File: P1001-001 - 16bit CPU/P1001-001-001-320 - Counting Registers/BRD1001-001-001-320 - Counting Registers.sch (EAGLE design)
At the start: 16 parts, among them IC1 74HC192D, IC12 74AC245DW, IC2 74HC192D, IC27 MEGA8535-A, IC3 74HC192D, IC4 74HC192D, IC5 74ALS04D, IC7 74AC245DW, J1 22-27-2041-04

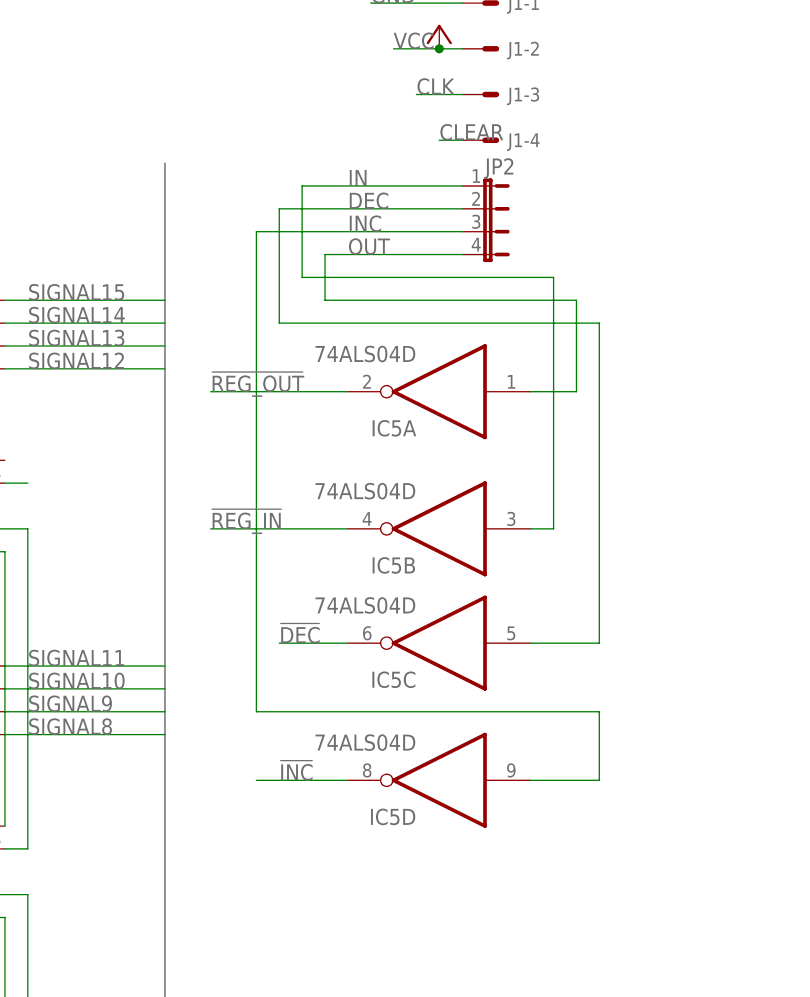
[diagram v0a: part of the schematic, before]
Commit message: Added the simple reg, cleaned things up
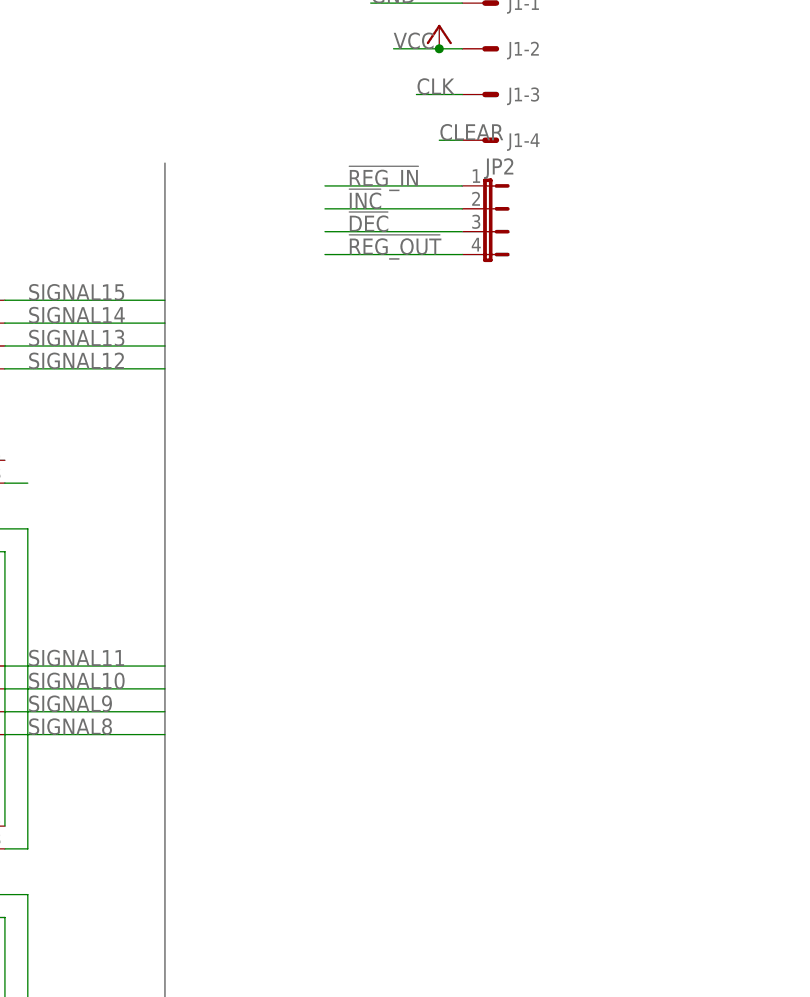
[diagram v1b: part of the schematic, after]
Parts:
- removed IC5: 74ALS04D, 74xx-us:74ALS04D
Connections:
- removed net DEC: IC5C.I, JP2.2
- removed net IN: IC5B.I, JP2.1
- removed net INC: IC5D.I, JP2.3
- removed net OUT: IC5A.I, JP2.4
- net !DEC: now also JP2.3; no longer IC5C.O
- net !INC: now also JP2.2; no longer IC5D.O
- net !REG_IN: now also JP2.1; no longer IC5B.O
- net !REG_OUT: now also JP2.4; no longer IC5A.O
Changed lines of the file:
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@@
 <class number="0" name="default" width="0" drill="0">
+</class>
+<class number="1" name="power" width="0.4572" drill="0">
 </class>
 </classes>
@@
 <part name="IC3" library="74xx-eu" library_urn="urn:adsk.eagle:library:85" deviceset="74*192" device="D" package3d_urn="urn:adsk.eagle:package:2010/1" technology="HC"/>
 <part name="IC4" library="74xx-eu" library_urn="urn:adsk.eagle:library:85" deviceset="74*192" device="D" package3d_urn="urn:adsk.eagle:package:2010/1" technology="HC"/>
-<part name="IC5" library="74xx-us" library_urn="urn:adsk.eagle:library:88" deviceset="74*04" device="D" package3d_urn="urn:adsk.eagle:package:2917/1" technology="ALS"/>
 </parts>
 <sheets>
@@
 <attribute name="VALUE" x="73.66" y="104.14" size="1.778" layer="96"/>
 </instance>
-<instance part="IC5" gate="A" x="142.24" y="119.38" smashed="yes" rot="R180">
-<attribute name="NAME" x="139.7" y="116.205" size="1.778" layer="95" rot="R180"/>
-<attribute name="VALUE" x="139.7" y="124.46" size="1.778" layer="96" rot="R180"/>
-</instance>
-<instance part="IC5" gate="B" x="142.24" y="104.14" smashed="yes" rot="R180">
-<attribute name="NAME" x="139.7" y="100.965" size="1.778" layer="95" rot="R180"/>
-<attribute name="VALUE" x="139.7" y="109.22" size="1.778" layer="96" rot="R180"/>
-</instance>
-<instance part="IC5" gate="C" x="142.24" y="91.44" smashed="yes" rot="R180">
-<attribute name="NAME" x="139.7" y="88.265" size="1.778" layer="95" rot="R180"/>
-<attribute name="VALUE" x="139.7" y="96.52" size="1.778" layer="96" rot="R180"/>
-</instance>
-<instance part="IC5" gate="D" x="142.24" y="76.2" smashed="yes" rot="R180">
-<attribute name="NAME" x="139.7" y="73.025" size="1.778" layer="95" rot="R180"/>
-<attribute name="VALUE" x="139.7" y="81.28" size="1.778" layer="96" rot="R180"/>
-</instance>
 </instances>
 <busses>
@@
 </segment>
 <segment>
-<pinref part="IC5" gate="A" pin="O"/>
-<wire x1="132.08" y1="119.38" x2="116.84" y2="119.38" width="0.1524" layer="91"/>
-<label x="116.84" y="119.38" size="1.778" layer="95"/>
+<pinref part="JP2" gate="G$1" pin="4"/>
+<wire x1="144.78" y1="134.62" x2="129.54" y2="134.62" width="0.1524" layer="91"/>
+<label x="132.08" y="134.62" size="1.778" layer="95"/>
 </segment>
 </net>
@@
 </segment>
 <segment>
-<pinref part="IC5" gate="B" pin="O"/>
-<wire x1="132.08" y1="104.14" x2="116.84" y2="104.14" width="0.1524" layer="91"/>
-<label x="116.84" y="104.14" size="1.778" layer="95"/>
-</segment>
-</net>
-<net name="GND" class="0">
+<pinref part="JP2" gate="G$1" pin="1"/>
+<wire x1="144.78" y1="142.24" x2="129.54" y2="142.24" width="0.1524" layer="91"/>
+<label x="132.08" y="142.24" size="1.778" layer="95"/>
+</segment>
+</net>
+<net name="GND" class="1">
 <segment>
 <pinref part="GND1" gate="1" pin="GND"/>
@@
 </segment>
 </net>
-<net name="VCC" class="0">
+<net name="VCC" class="1">
 <segment>
 <pinref part="J1" gate="-2" pin="S"/>
@@
 </segment>
 </net>
-<net name="DEC" class="0">
-<segment>
-<pinref part="JP2" gate="G$1" pin="2"/>
-<wire x1="144.78" y1="139.7" x2="124.46" y2="139.7" width="0.1524" layer="91"/>
-<label x="132.08" y="139.7" size="1.778" layer="95"/>
-<wire x1="124.46" y1="139.7" x2="124.46" y2="127" width="0.1524" layer="91"/>
-<wire x1="124.46" y1="127" x2="160.02" y2="127" width="0.1524" layer="91"/>
-<pinref part="IC5" gate="C" pin="I"/>
-<wire x1="160.02" y1="127" x2="160.02" y2="91.44" width="0.1524" layer="91"/>
-<wire x1="160.02" y1="91.44" x2="152.4" y2="91.44" width="0.1524" layer="91"/>
-</segment>
-</net>
-<net name="INC" class="0">
-<segment>
-<pinref part="JP2" gate="G$1" pin="3"/>
-<wire x1="144.78" y1="137.16" x2="121.92" y2="137.16" width="0.1524" layer="91"/>
-<label x="132.08" y="137.16" size="1.778" layer="95"/>
-<wire x1="121.92" y1="137.16" x2="121.92" y2="83.82" width="0.1524" layer="91"/>
-<wire x1="121.92" y1="83.82" x2="160.02" y2="83.82" width="0.1524" layer="91"/>
-<wire x1="160.02" y1="83.82" x2="160.02" y2="76.2" width="0.1524" layer="91"/>
-<pinref part="IC5" gate="D" pin="I"/>
-<wire x1="160.02" y1="76.2" x2="152.4" y2="76.2" width="0.1524" layer="91"/>
-</segment>
-</net>
 <net name="N$1" class="0">
 <segment>
 <pinref part="IC4" gate="A" pin="BO"/>
 <wire x1="96.52" y1="109.22" x2="93.98" y2="109.22" width="0.1524" layer="91"/>
-</segment>
-</net>
-<net name="IN" class="0">
-<segment>
-<pinref part="JP2" gate="G$1" pin="1"/>
-<wire x1="144.78" y1="142.24" x2="127" y2="142.24" width="0.1524" layer="91"/>
-<label x="132.08" y="142.24" size="1.778" layer="95"/>
-<wire x1="127" y1="142.24" x2="127" y2="132.08" width="0.1524" layer="91"/>
-<wire x1="127" y1="132.08" x2="154.94" y2="132.08" width="0.1524" layer="91"/>
-<wire x1="154.94" y1="132.08" x2="154.94" y2="104.14" width="0.1524" layer="91"/>
-<pinref part="IC5" gate="B" pin="I"/>
-<wire x1="154.94" y1="104.14" x2="152.4" y2="104.14" width="0.1524" layer="91"/>
-</segment>
-</net>
-<net name="OUT" class="0">
-<segment>
-<pinref part="JP2" gate="G$1" pin="4"/>
-<wire x1="144.78" y1="134.62" x2="129.54" y2="134.62" width="0.1524" layer="91"/>
-<label x="132.08" y="134.62" size="1.778" layer="95"/>
-<wire x1="129.54" y1="134.62" x2="129.54" y2="129.54" width="0.1524" layer="91"/>
-<wire x1="129.54" y1="129.54" x2="157.48" y2="129.54" width="0.1524" layer="91"/>
-<wire x1="157.48" y1="129.54" x2="157.48" y2="119.38" width="0.1524" layer="91"/>
-<pinref part="IC5" gate="A" pin="I"/>
-<wire x1="157.48" y1="119.38" x2="152.4" y2="119.38" width="0.1524" layer="91"/>
 </segment>
 </net>
@@
 </segment>
 <segment>
-<pinref part="IC5" gate="C" pin="O"/>
-<wire x1="132.08" y1="91.44" x2="124.46" y2="91.44" width="0.1524" layer="91"/>
-<label x="124.46" y="91.44" size="1.778" layer="95"/>
+<pinref part="JP2" gate="G$1" pin="3"/>
+<wire x1="144.78" y1="137.16" x2="129.54" y2="137.16" width="0.1524" layer="91"/>
+<label x="132.08" y="137.16" size="1.778" layer="95"/>
 </segment>
 </net>
@@
 </segment>
 <segment>
-<pinref part="IC5" gate="D" pin="O"/>
-<wire x1="132.08" y1="76.2" x2="121.92" y2="76.2" width="0.1524" layer="91"/>
-<label x="124.46" y="76.2" size="1.778" layer="95"/>
-</segment>
-</net>
+<pinref part="JP2" gate="G$1" pin="2"/>
+<wire x1="144.78" y1="139.7" x2="129.54" y2="139.7" width="0.1524" layer="91"/>
+<label x="132.08" y="139.7" size="1.778" layer="95"/>
+</segment>
+</net>

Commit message: Finished All Boards
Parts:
- added C1, C2, C3, C4: 1uF, rcl:C-USC1206
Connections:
- net GND: now also C1.2, C2.2, C3.2, C4.2
- net VCC: now also C1.1, C2.1, C3.1, C4.1

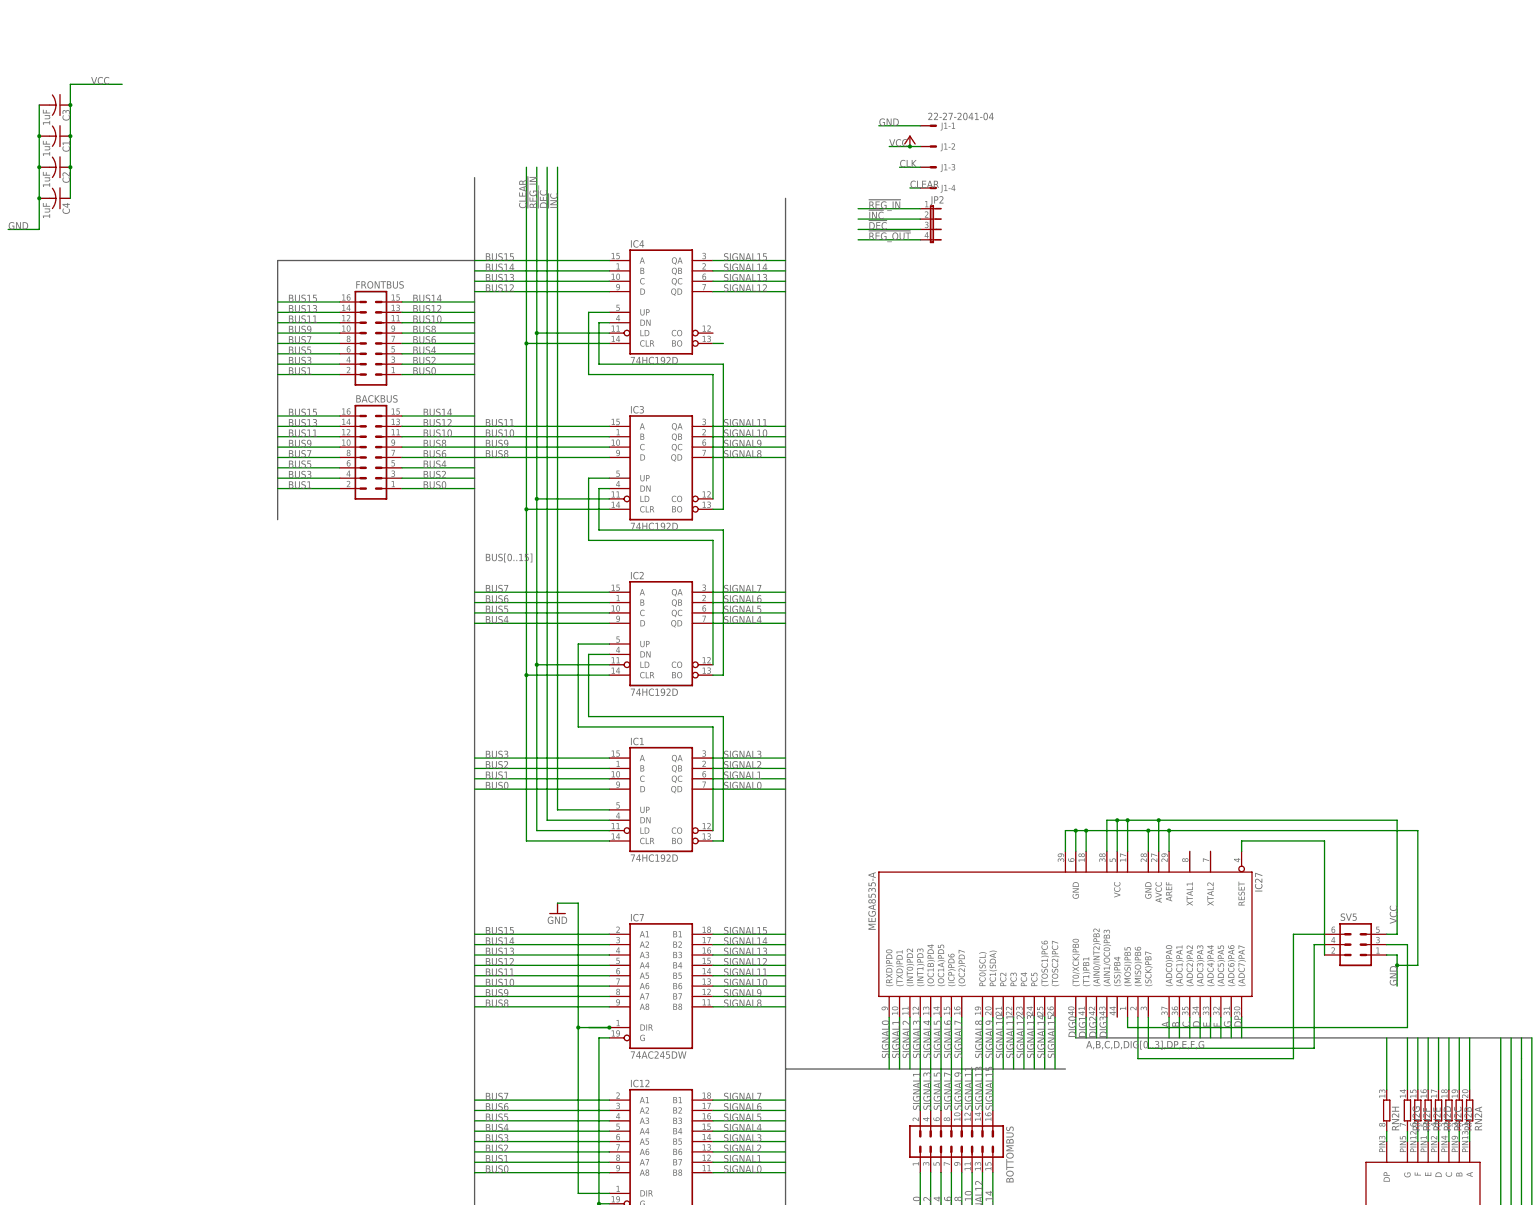
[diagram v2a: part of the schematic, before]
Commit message: fix the 16 register problem
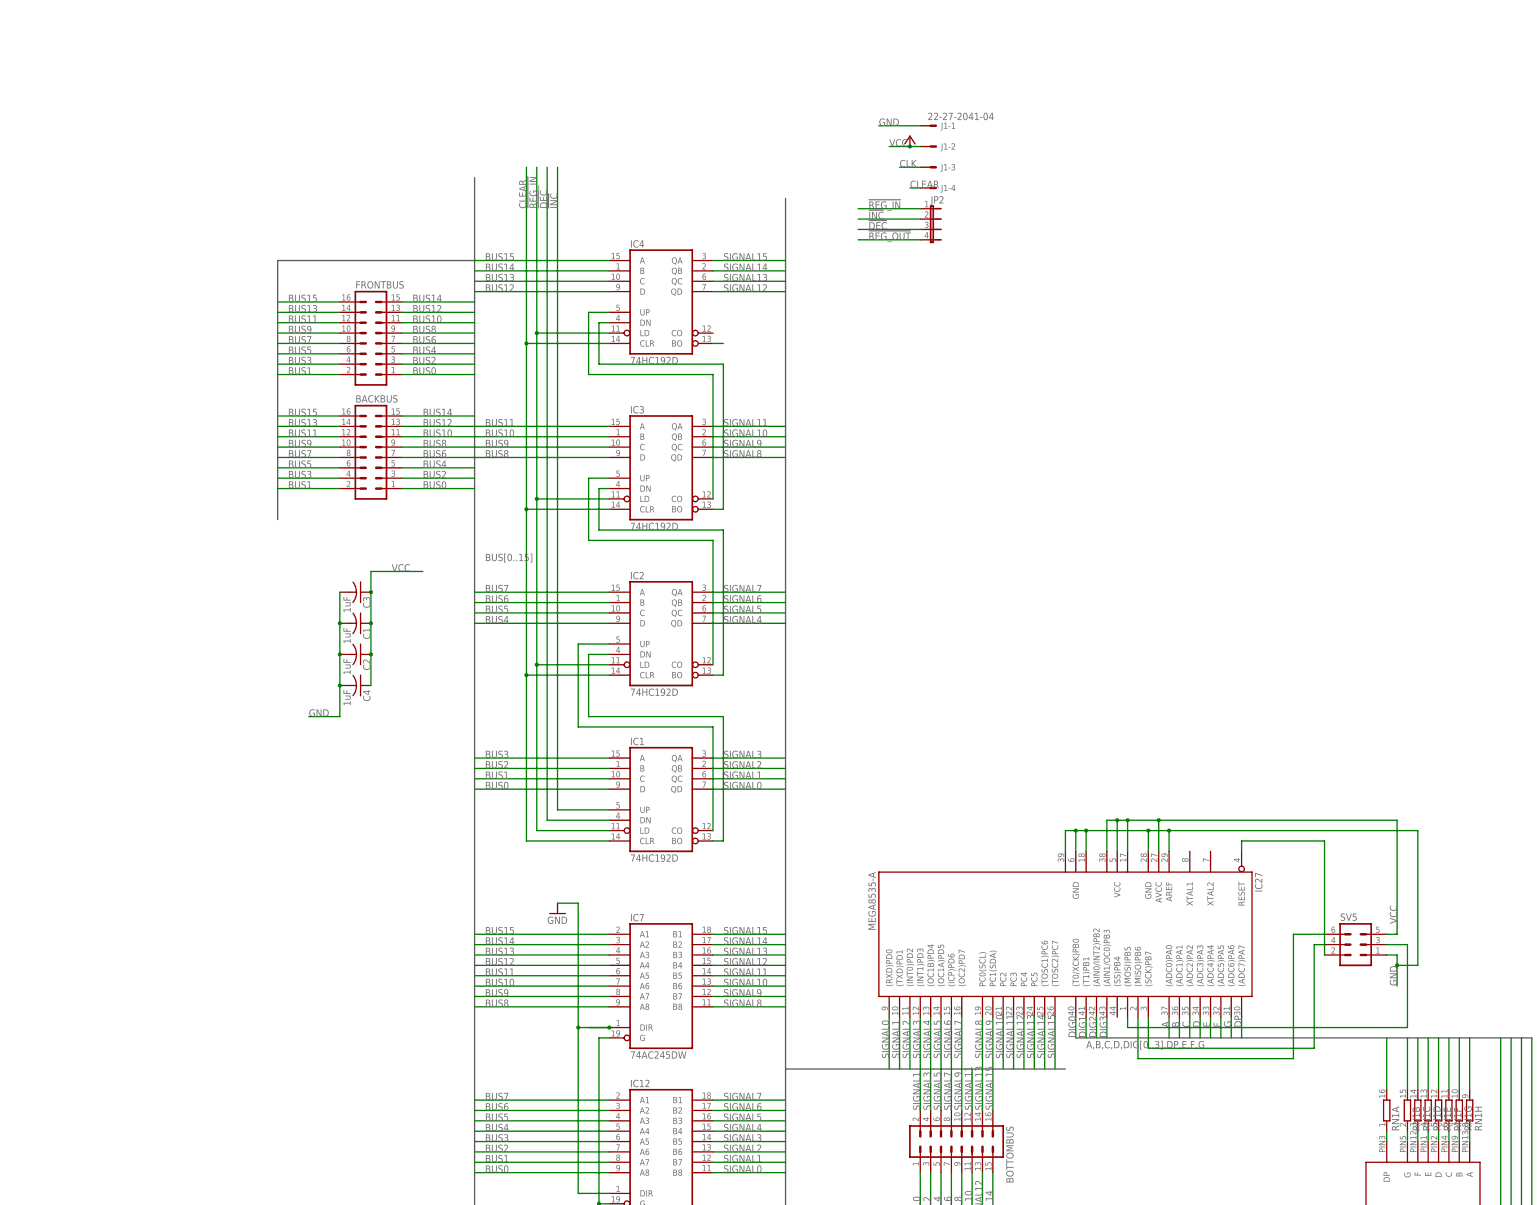
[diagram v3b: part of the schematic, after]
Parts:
- removed RN2: (no value), resistor-dil:10R-NSOMC
- added RN1: (no value), resistor-dil:8R-NSOMC
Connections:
- net A: now also RN1H.2; no longer RN2A.2
- net B: now also RN1G.2; no longer RN2B.2
- net C: now also RN1F.2; no longer RN2C.2
- net D: now also RN1E.2; no longer RN2D.2
- net DP: now also RN1A.2; no longer RN2H.2
- net E: now also RN1D.2; no longer RN2E.2
- net F: now also RN1C.2; no longer RN2F.2
- net G: now also RN1B.2; no longer RN2G.2
- net N$24: now also RN1H.1; no longer RN2A.1
- net N$25: now also RN1G.1; no longer RN2B.1
- net N$26: now also RN1F.1; no longer RN2C.1
- net N$27: now also RN1E.1; no longer RN2D.1
- net N$28: now also RN1D.1; no longer RN2E.1
- net N$29: now also RN1C.1; no longer RN2F.1
- net N$30: now also RN1B.1; no longer RN2G.1
- net N$31: now also RN1A.1; no longer RN2H.1
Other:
- moved on the sheet: C1, C2, C3, C4
